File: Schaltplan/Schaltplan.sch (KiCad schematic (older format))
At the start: 12 parts, among them IC1 STM32G031J6M6, J1 Conn_01x01, J2 Conn_02x03_Odd_Even, SW1 SW_SPDT, U1 HU2032-LF

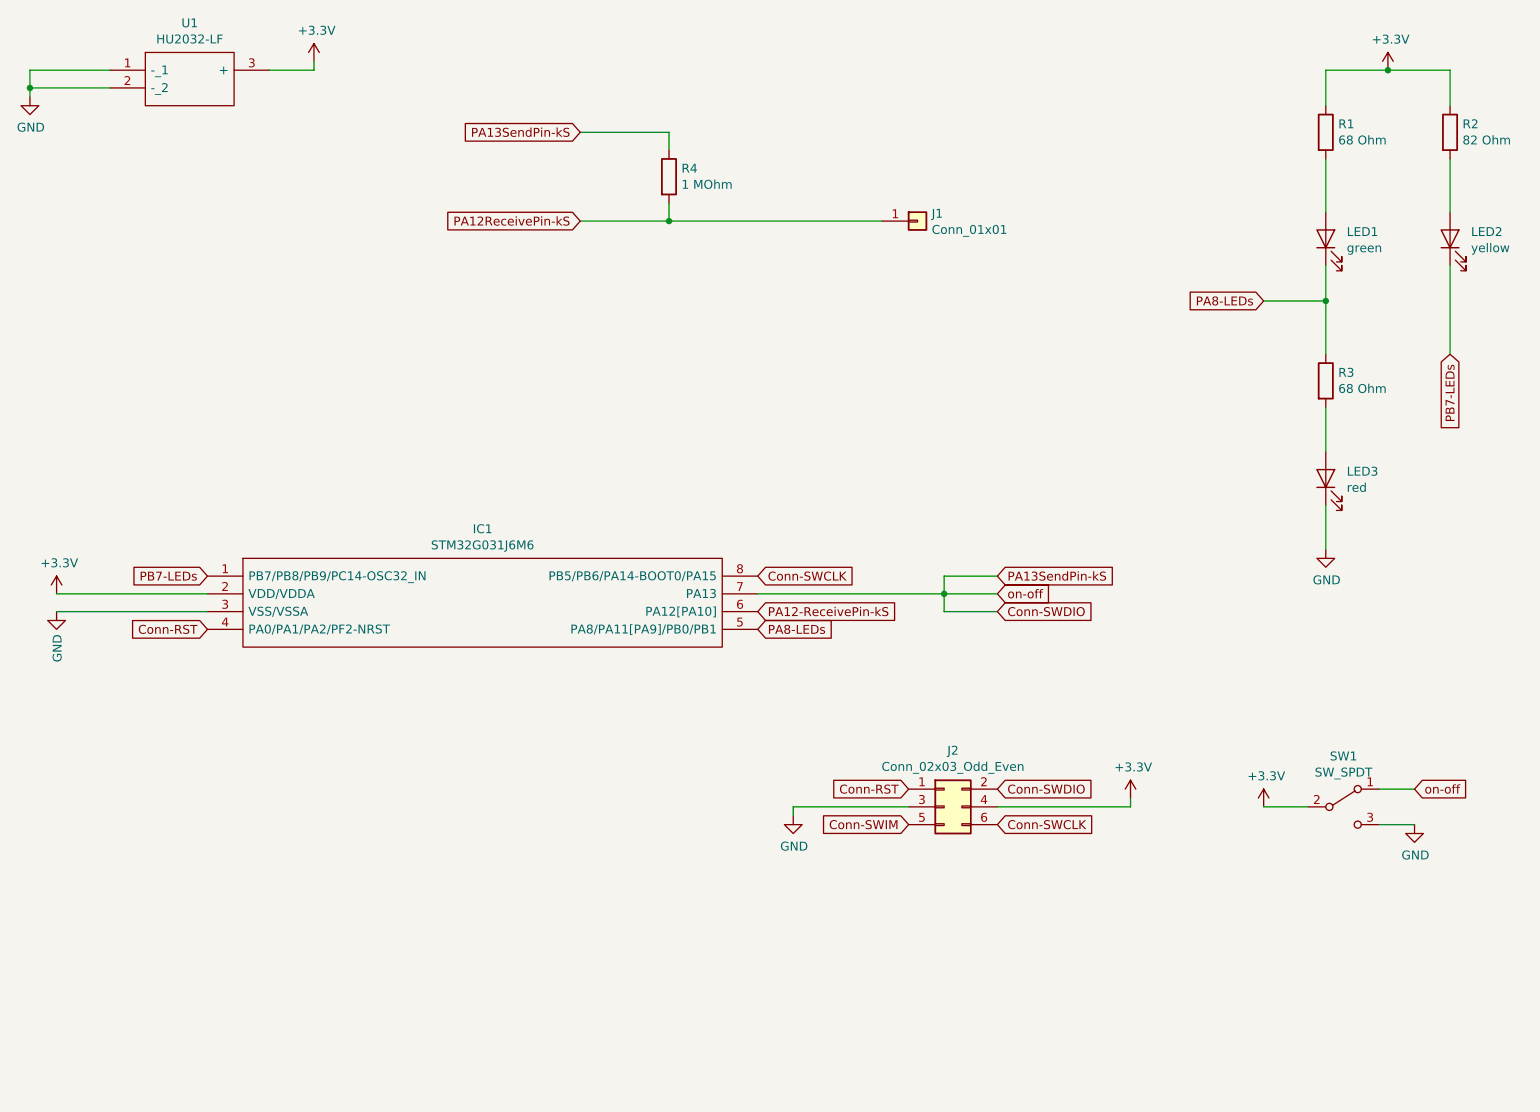
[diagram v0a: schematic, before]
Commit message: ersten Leiterbahnen gezogen
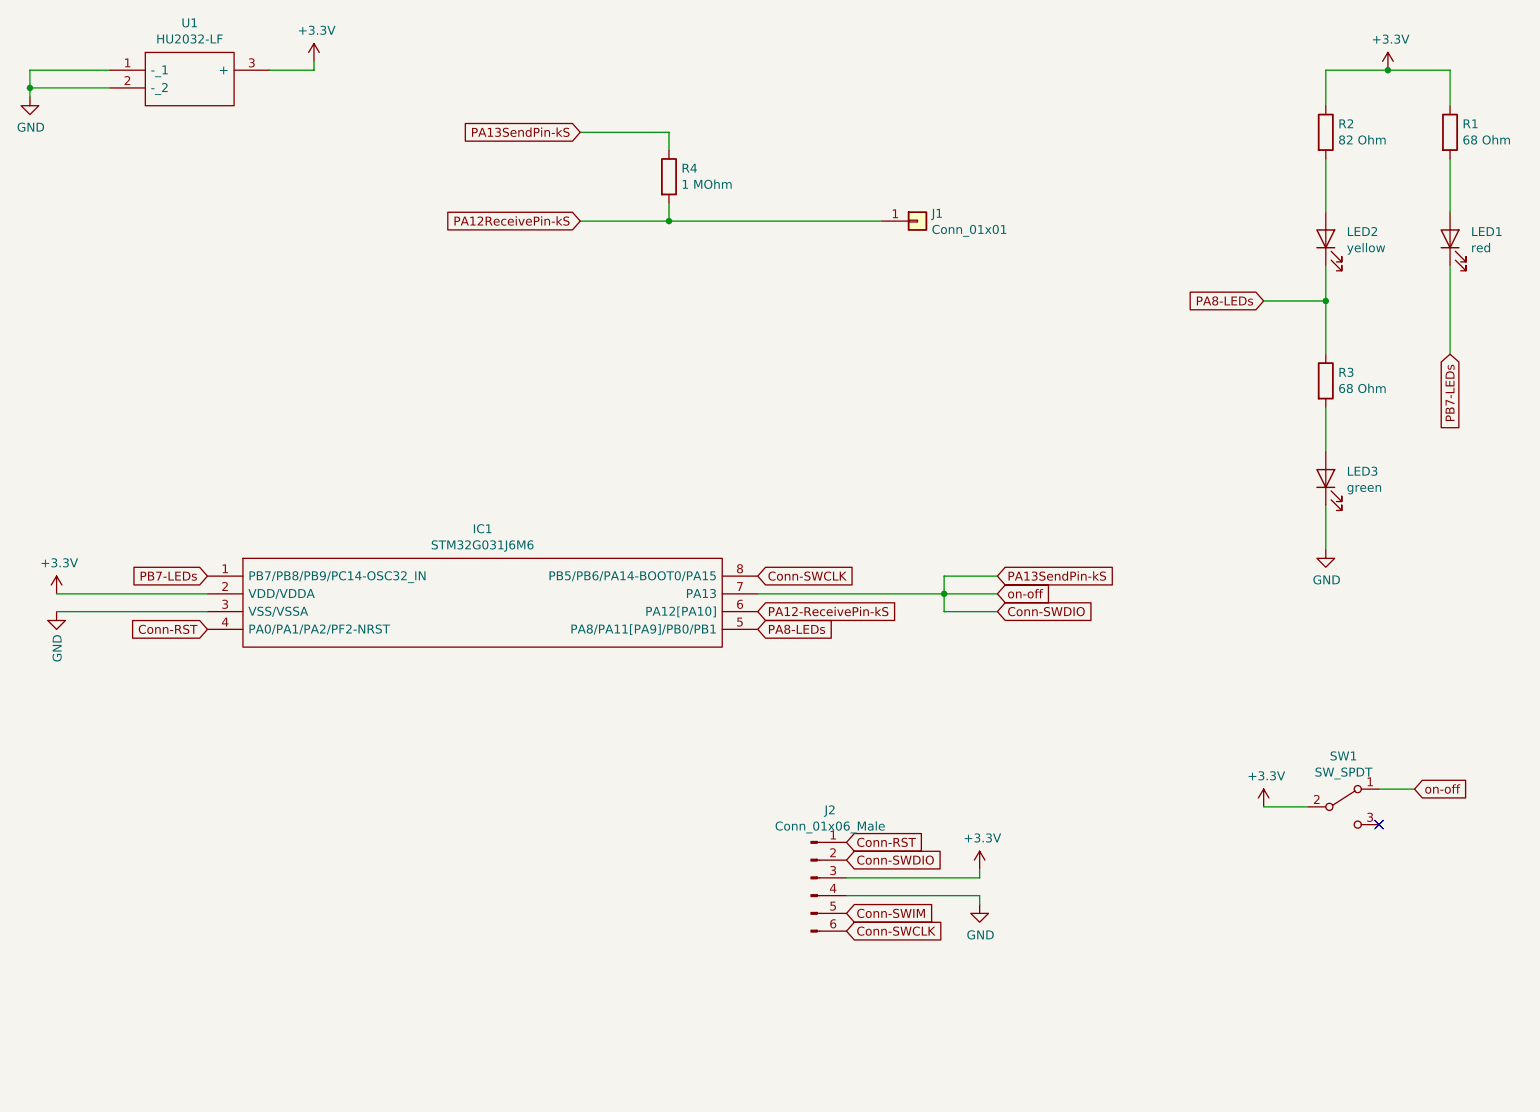
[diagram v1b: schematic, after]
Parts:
- removed J2: Conn_02x03_Odd_Even, Connector_PinHeader_2.54mm:PinHeader_2x03_P2.54mm_Vertical, symbol Connector_Generic:Conn_02x03_Odd_Even
- added J2: Conn_01x06_Male, Connector_PinHeader_2.54mm:PinHeader_1x06_P2.54mm_Vertical, symbol Connector:Conn_01x06_Male
- LED1: renamed from LED2; value yellow -> red
- LED2: renamed from LED1; value green -> yellow
- LED3: value red -> green
- R1: renamed from R2; value 82 Ohm -> 68 Ohm
- R2: renamed from R1; value 68 Ohm -> 82 Ohm
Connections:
- net +3V3: now also J2.3 (Pin_3)
- net Conn-RST: now also J2.1 (Pin_1)
- net Conn-SWCLK: now also J2.6 (Pin_6)
- net Conn-SWDIO: now also J2.2 (Pin_2)
- net Conn-SWIM: now also J2.5 (Pin_5)
- net GND: now also J2.4 (Pin_4); no longer SW1.3 (C)
- no-connect marks 0 -> 1
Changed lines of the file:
@@
 $EndComp
 $Comp
-L Device:R R1
+L Device:R R2
 U 1 1 5EE3B4D7
 P 8400 1700
-F 0 "R1" H 8470 1746 50  0000 L CNN
-F 1 "68 Ohm" H 8470 1655 50  0000 L CNN
+F 0 "R2" H 8470 1746 50  0000 L CNN
+F 1 "82 Ohm" H 8470 1655 50  0000 L CNN
 F 2 "Resistor_THT:R_Axial_DIN0411_L9.9mm_D3.6mm_P20.32mm_Horizontal" V 8330 1700 50  0001 C CNN
 F 3 "~" H 8400 1700 50  0001 C CNN
@@
 $EndComp
 $Comp
-L Device:LED LED1
+L Device:LED LED2
 U 1 1 5EE899FD
 P 8400 2300
-F 0 "LED1" V 8439 2182 50  0000 R CNN
-F 1 "green" V 8348 2182 50  0000 R CNN
+F 0 "LED2" V 8439 2182 50  0000 R CNN
+F 1 "yellow" V 8348 2182 50  0000 R CNN
 F 2 "LED_THT:LED_D5.0mm" H 8400 2300 50  0001 C CNN
 F 3 "~" H 8400 2300 50  0001 C CNN
@@
 P 8400 3650
 F 0 "LED3" V 8439 3532 50  0000 R CNN
-F 1 "red" V 8348 3532 50  0000 R CNN
+F 1 "green" V 8348 3532 50  0000 R CNN
 F 2 "LED_THT:LED_D5.0mm" H 8400 3650 50  0001 C CNN
 F 3 "~" H 8400 3650 50  0001 C CNN
@@
 $EndComp
 $Comp
-L Device:LED LED2
+L Device:LED LED1
 U 1 1 5EE8A614
 P 9100 2300
-F 0 "LED2" V 9139 2182 50  0000 R CNN
-F 1 "yellow" V 9048 2182 50  0000 R CNN
+F 0 "LED1" V 9139 2182 50  0000 R CNN
+F 1 "red" V 9048 2182 50  0000 R CNN
 F 2 "LED_THT:LED_D5.0mm" H 9100 2300 50  0001 C CNN
 F 3 "~" H 9100 2300 50  0001 C CNN
@@
 $EndComp
 $Comp
-L Device:R R2
+L Device:R R1
 U 1 1 5EE8AD00
 P 9100 1700
-F 0 "R2" H 9170 1746 50  0000 L CNN
-F 1 "82 Ohm" H 9170 1655 50  0000 L CNN
+F 0 "R1" H 9170 1746 50  0000 L CNN
+F 1 "68 Ohm" H 9170 1655 50  0000 L CNN
 F 2 "Resistor_THT:R_Axial_DIN0411_L9.9mm_D3.6mm_P20.32mm_Horizontal" V 9030 1700 50  0001 C CNN
 F 3 "~" H 9100 1700 50  0001 C CNN
@@
 Wire Wire Line
 	8300 5500 8050 5500
-$Comp
-L power:GND #PWR0108
-U 1 1 5EF44D1B
-P 8900 5600
-F 0 "#PWR0108" H 8900 5350 50  0001 C CNN
-F 1 "GND" H 8905 5427 50  0000 C CNN
-F 2 "" H 8900 5600 50  0001 C CNN
-F 3 "" H 8900 5600 50  0001 C CNN
-	1    8900 5600
-	1    0    0    -1
-$EndComp
-Wire Wire Line
-	8700 5600 8900 5600
 Text GLabel 8900 5400 2    50   Input ~ 0
 on-off
@@
 Text GLabel 6550 4300 2    50   Input ~ 0
 on-off
-$Comp
-L Connector_Generic:Conn_02x03_Odd_Even J2
-U 1 1 5EF4D1CC
-P 6250 5500
-F 0 "J2" H 6300 5817 50  0000 C CNN
-F 1 "Conn_02x03_Odd_Even" H 6300 5726 50  0000 C CNN
-F 2 "Connector_PinHeader_2.54mm:PinHeader_2x03_P2.54mm_Vertical" H 6250 5500 50  0001 C CNN
-F 3 "~" H 6250 5500 50  0001 C CNN
-	1    6250 5500
-	1    0    0    -1
-$EndComp
-Text GLabel 6050 5400 0    50   Input ~ 0
+Text GLabel 5700 5700 2    50   Input ~ 0
 Conn-RST
-Text GLabel 6050 5600 0    50   Input ~ 0
+Text GLabel 5700 6100 2    50   Input ~ 0
 Conn-SWIM
-Text GLabel 6550 5400 2    50   Input ~ 0
+Text GLabel 5700 5800 2    50   Input ~ 0
 Conn-SWDIO
-Text GLabel 6550 5600 2    50   Input ~ 0
+Text GLabel 5700 6200 2    50   Input ~ 0
 Conn-SWCLK
 $Comp
 L power:+3.3V #PWR0109
 U 1 1 5EF4F375
-P 7300 5450
-F 0 "#PWR0109" H 7300 5300 50  0001 C CNN
-F 1 "+3.3V" H 7315 5623 50  0000 C CNN
-F 2 "" H 7300 5450 50  0001 C CNN
-F 3 "" H 7300 5450 50  0001 C CNN
-	1    7300 5450
+P 6450 5850
+F 0 "#PWR0109" H 6450 5700 50  0001 C CNN
+F 1 "+3.3V" H 6465 6023 50  0000 C CNN
+F 2 "" H 6450 5850 50  0001 C CNN
+F 3 "" H 6450 5850 50  0001 C CNN
+	1    6450 5850
 	1    0    0    -1
 $EndComp
@@
 L power:GND #PWR0110
 U 1 1 5EF4FC6C
-P 5400 5550
-F 0 "#PWR0110" H 5400 5300 50  0001 C CNN
-F 1 "GND" H 5405 5377 50  0000 C CNN
-F 2 "" H 5400 5550 50  0001 C CNN
-F 3 "" H 5400 5550 50  0001 C CNN
-	1    5400 5550
-	1    0    0    -1
-$EndComp
-Wire Wire Line
-	6050 5500 5400 5500
-Wire Wire Line
-	5400 5500 5400 5550
-Wire Wire Line
-	7300 5450 7300 5500
-Wire Wire Line
-	7300 5500 6550 5500
+P 6450 6050
+F 0 "#PWR0110" H 6450 5800 50  0001 C CNN
+F 1 "GND" H 6455 5877 50  0000 C CNN
+F 2 "" H 6450 6050 50  0001 C CNN
+F 3 "" H 6450 6050 50  0001 C CNN
+	1    6450 6050
+	1    0    0    -1
+$EndComp
+Wire Wire Line
+	6450 6000 6450 6050
+Wire Wire Line
+	6450 5850 6450 5900
+Wire Wire Line
+	6450 6000 5700 6000
 Text GLabel 6550 4400 2    50   Input ~ 0
 Conn-SWDIO
@@
 Wire Wire Line
 	6250 4400 6550 4400
+NoConn ~ 8700 5600
+$Comp
+L Connector:Conn_01x06_Male J2
+U 1 1 5EF9CAFA
+P 5500 5900
+F 0 "J2" H 5608 6281 50  0000 C CNN
+F 1 "Conn_01x06_Male" H 5608 6190 50  0000 C CNN
+F 2 "Connector_PinHeader_2.54mm:PinHeader_1x06_P2.54mm_Vertical" H 5500 5900 50  0001 C CNN
+F 3 "~" H 5500 5900 50  0001 C CNN
+	1    5500 5900
+	1    0    0    -1
+$EndComp
+Wire Wire Line
+	5700 5900 6450 5900
 $EndSCHEMATC

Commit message: mit button Kupfer und Design Check
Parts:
- added H1, H2, H3: MountingHole, MountingHole:MountingHole_4.5mm, symbol Mechanical:MountingHole
- J1: footprint Connector_Phoenix_MSTB:PhoenixContact_MSTBA_2,5_2-G-5,08_1x02_P5.08mm_Horizontal -> Connector_PinHeader_2.54mm:PinHeader_1x01_P2.54mm_Vertical
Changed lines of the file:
@@
 F 0 "J1" H 6180 2242 50  0000 L CNN
 F 1 "Conn_01x01" H 6180 2151 50  0000 L CNN
-F 2 "Connector_Phoenix_MSTB:PhoenixContact_MSTBA_2,5_2-G-5,08_1x02_P5.08mm_Horizontal" H 6100 2200 50  0001 C CNN
+F 2 "Connector_PinHeader_2.54mm:PinHeader_1x01_P2.54mm_Vertical" H 6100 2200 50  0001 C CNN
 F 3 "~" H 6100 2200 50  0001 C CNN
 	1    6100 2200
@@
 Wire Wire Line
 	5700 5900 6450 5900
+$Comp
+L Mechanical:MountingHole H1
+U 1 1 5EFC65F8
+P 1750 6550
+F 0 "H1" H 1850 6596 50  0000 L CNN
+F 1 "MountingHole" H 1850 6505 50  0000 L CNN
+F 2 "MountingHole:MountingHole_4.5mm" H 1750 6550 50  0001 C CNN
+F 3 "~" H 1750 6550 50  0001 C CNN
+	1    1750 6550
+	1    0    0    -1
+$EndComp
+$Comp
+L Mechanical:MountingHole H2
+U 1 1 5EFC738C
+P 2500 6550
+F 0 "H2" H 2600 6596 50  0000 L CNN
+F 1 "MountingHole" H 2600 6505 50  0000 L CNN
+F 2 "MountingHole:MountingHole_4.5mm" H 2500 6550 50  0001 C CNN
+F 3 "~" H 2500 6550 50  0001 C CNN
+	1    2500 6550
+	1    0    0    -1
+$EndComp
+$Comp
+L Mechanical:MountingHole H3
+U 1 1 5EFC7750
+P 3200 6550
+F 0 "H3" H 3300 6596 50  0000 L CNN
+F 1 "MountingHole" H 3300 6505 50  0000 L CNN
+F 2 "MountingHole:MountingHole_4.5mm" H 3200 6550 50  0001 C CNN
+F 3 "~" H 3200 6550 50  0001 C CNN
+	1    3200 6550
+	1    0    0    -1
+$EndComp
 $EndSCHEMATC
